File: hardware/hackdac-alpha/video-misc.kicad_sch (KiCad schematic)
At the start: 43 parts, among them J2 TTL SYNC, J3 SYNC OUT, P1 BANK2_AUX, Q1 2N7002, Q2 BC847, Q3 BC857, Q4 BC857, U5 MCP47FEB22A1-E/ST, U6 74LVCH16T245, U7 74LVC1G125, X1 ECS-TXO-3225-270-TR

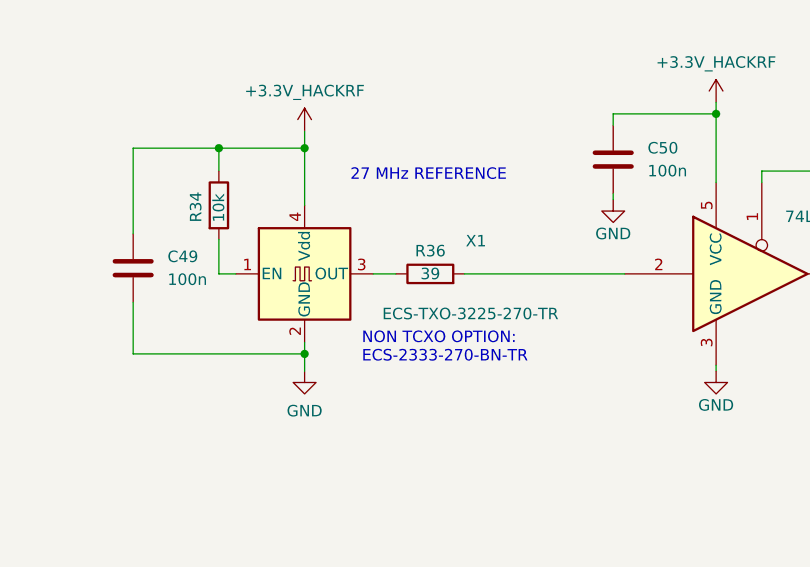
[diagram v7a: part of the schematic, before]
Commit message: Changed X1 to 5x3.2mm footprint
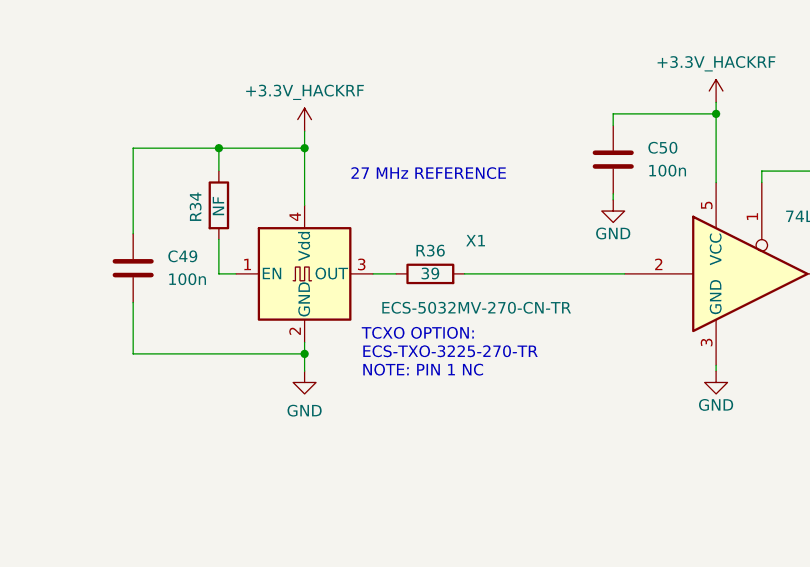
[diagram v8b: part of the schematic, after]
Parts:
- R34: value 10k -> NF
- X1: value ECS-TXO-3225-270-TR -> ECS-5032MV-270-CN-TR; footprint Oscillator:Oscillator_SMD_EuroQuartz_XO32-4Pin_3.2x2.5mm -> Oscillator:Oscillator_SMD_EuroQuartz_XO53-4Pin_5.0x3.2mm
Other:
- note added: "TCXO OPTION: ECS-TXO-3225-270-TR NOTE: PIN 1 NC"
- note removed: "NON TCXO OPTION: ECS-2333-270-BN-TR"
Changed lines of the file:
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@@
 		)
 	)
-	(text "NON TCXO OPTION:\nECS-2333-270-BN-TR"
+	(text "TCXO OPTION:\nECS-TXO-3225-270-TR\nNOTE: PIN 1 NC"
 		(exclude_from_sim no)
-		(at 193.675 139.7 0)
+		(at 193.675 140.335 0)
 		(effects
 			(font
@@
 			)
 		)
-		(property "Value" "10k"
-			(at 177.8 125.73 90)
+		(property "Value" "NF"
+			(at 177.8 125.095 90)
 			(effects
 				(font
@@
 			)
 		)
-		(property "Value" "ECS-TXO-3225-270-TR"
-			(at 205.74 135.89 0)
+		(property "Value" "ECS-5032MV-270-CN-TR"
+			(at 206.375 135.255 0)
 			(effects
 				(font
@@
 			)
 		)
-		(property "Footprint" "Oscillator:Oscillator_SMD_EuroQuartz_XO32-4Pin_3.2x2.5mm"
+		(property "Footprint" "Oscillator:Oscillator_SMD_EuroQuartz_XO53-4Pin_5.0x3.2mm"
 			(at 205.105 140.335 0)
 			(effects
